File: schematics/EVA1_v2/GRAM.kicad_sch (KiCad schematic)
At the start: 8 parts, among them U11 CY62256-70PC, U25 74LS157, U26 74LS157, U27 74LS157, U28 74LS157, U35 74LS165, U36 74LS245, U38 74LS573

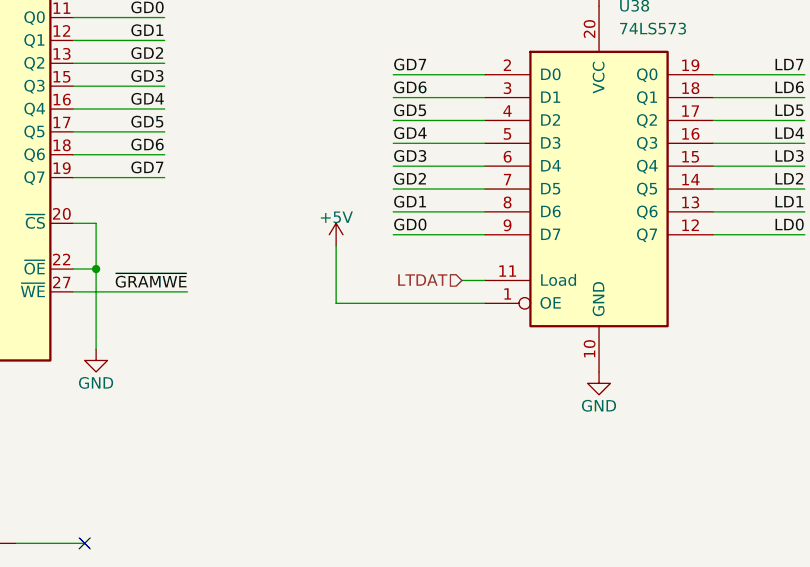
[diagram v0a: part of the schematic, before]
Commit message: schematics updated
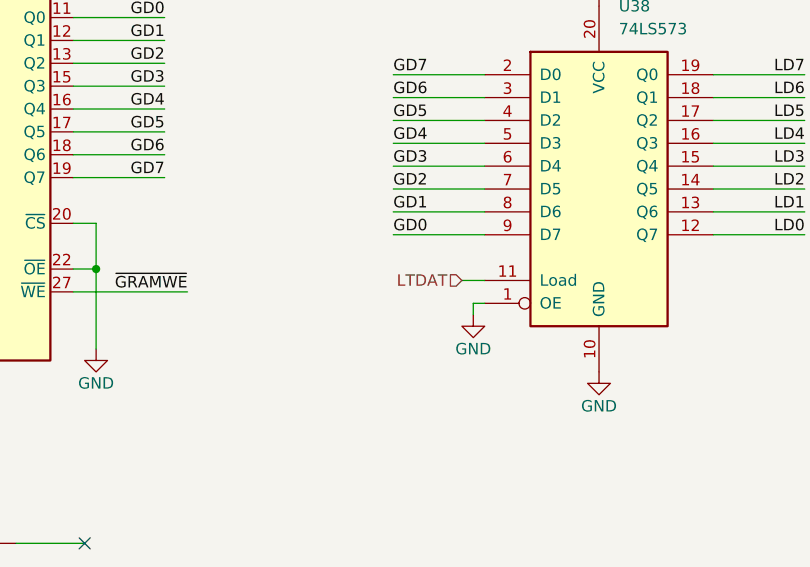
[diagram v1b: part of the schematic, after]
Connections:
- net +5V: no longer U38.1 (OE)
- net GND: now also U38.1 (OE)
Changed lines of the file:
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@@
 		(title "EVA1 (Epson Video Adapter) - Graphic RAM")
 		(date "2025-01-09")
-		(rev "v0.1")
+		(rev "v0.3")
 		(company "100% Offner")
 		(comment 1 "v0.1: Initial Release")
+		(comment 2 "v0.2: Production version")
+		(comment 3 "v0.3: Redesign with SRAM")
 	)
 	(junction
@@
 	(wire
 		(pts
-			(xy 226.06 55.88) (xy 209.55 55.88)
+			(xy 226.06 55.88) (xy 224.79 55.88)
 		)
 		(stroke
@@
 	(wire
 		(pts
-			(xy 209.55 49.53) (xy 209.55 55.88)
-		)
-		(stroke
-			(width 0)
-			(type default)
-		)
-	)
-	(wire
-		(pts
 			(xy 180.34 24.13) (xy 190.5 24.13)
 		)
@@
 	(wire
 		(pts
+			(xy 224.79 55.88) (xy 224.79 57.15)
+		)
+		(stroke
+			(width 0)
+			(type default)
+		)
+	)
+	(wire
+		(pts
 			(xy 180.34 54.61) (xy 193.04 54.61)
 		)
@@
 	(symbol
 		(lib_id "power:GND")
+		(at 224.79 57.15 0)
+		(unit 1)
+		(exclude_from_sim no)
+		(in_bom yes)
+		(on_board yes)
+		(dnp no)
+		(property "Reference" "#PWR70"
+			(at 224.79 63.5 0)
+			(effects
+				(font
+					(size 1.27 1.27)
+				)
+				(hide yes)
+			)
+		)
+		(property "Value" "GND"
+			(at 224.79 60.96 0)
+			(effects
+				(font
+					(size 1.27 1.27)
+				)
+			)
+		)
+		(property "Footprint" ""
+			(at 224.79 57.15 0)
+			(effects
+				(font
+					(size 1.27 1.27)
+				)
+				(hide yes)
+			)
+		)
+		(property "Datasheet" ""
+			(at 224.79 57.15 0)
+			(effects
+				(font
+					(size 1.27 1.27)
+				)
+				(hide yes)
+			)
+		)
+		(property "Description" ""
+			(at 224.79 57.15 0)
+			(effects
+				(font
+					(size 1.27 1.27)
+				)
+				(hide yes)
+			)
+		)
+		(pin "1"
+		)
+		(instances
+			(project "EVA1_v2"
+				(path "/5be3a086-9309-43f4-b37c-0519e88c3e26/4b69d599-71e1-4fe9-8a9f-9911911cdfa3"
+					(reference "#PWR70")
+					(unit 1)
+				)
+			)
+		)
+	)
+	(symbol
+		(lib_id "power:GND")
 		(at 114.3 67.31 0)
 		(unit 1)
@@
 					(unit 1)
 				)
-			)
-		)
-	)
-	(symbol
-		(lib_id "power:+5V")
-		(at 209.55 49.53 0)
-		(unit 1)
-		(exclude_from_sim no)
-		(in_bom yes)
-		(on_board yes)
-		(dnp no)
-		(property "Reference" "#PWR162"
-			(at 209.55 53.34 0)
-			(effects
-				(font
-					(size 1.27 1.27)
-				)
-				(hide yes)
-			)
-		)
-		(property "Value" "+5V"
-			(at 209.55 46.355 0)
-			(effects
-				(font
-					(size 1.27 1.27)
-				)
-			)
-		)
-		(property "Footprint" ""
-			(at 209.55 49.53 0)
-			(effects
-				(font
-					(size 1.27 1.27)
-				)
-				(hide yes)
-			)
-		)
-		(property "Datasheet" ""
-			(at 209.55 49.53 0)
-			(effects
-				(font
-					(size 1.27 1.27)
-				)
-				(hide yes)
-			)
-		)
-		(property "Description" ""
-			(at 209.55 49.53 0)
-			(effects
-				(font
-					(size 1.27 1.27)
-				)
-				(hide yes)
-			)
-		)
-		(pin "1"
-		)
-		(instances
-			(project "EVA1_v2"
-				(path "/5be3a086-9309-43f4-b37c-0519e88c3e26/4b69d599-71e1-4fe9-8a9f-9911911cdfa3"
-					(reference "#PWR162")
-					(unit 1)
-				)

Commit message: Schematic and Board updated
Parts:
- U25, U26, U27, U28: value 74LS157 -> 74ALS157
- U35: value 74LS165 -> 74HCT165
- U36: value 74LS245 -> 74HCT245
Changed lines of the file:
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@@
 			)
 		)
-		(property "Value" "74LS157"
+		(property "Value" "74ALS157"
 			(at 119.0341 128.27 0)
 			(effects
@@
 			)
 		)
-		(property "Value" "74LS245"
+		(property "Value" "74HCT245"
 			(at 211.7441 105.41 0)
 			(effects
@@
 			)
 		)
-		(property "Value" "74LS157"
+		(property "Value" "74ALS157"
 			(at 163.4841 78.74 0)
 			(effects
@@
 			)
 		)
-		(property "Value" "74LS157"
+		(property "Value" "74ALS157"
 			(at 116.4941 22.86 0)
 			(effects
@@
 			)
 		)
-		(property "Value" "74LS157"
+		(property "Value" "74ALS157"
 			(at 112.6841 77.47 0)
 			(effects
@@
 			)
 		)
-		(property "Value" "74LS165"
+		(property "Value" "74HCT165"
 			(at 265.0841 113.03 0)
 			(effects

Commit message: new Gerber files
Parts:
- removed U38: 74LS573, Package_DIP:DIP-20_W7.62mm, symbol 74xx:74LS573
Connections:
- net LD0 is gone; now on net GD0: U35.11 (D0)
- net LD1 is gone; now on net GD1: U35.12 (D1)
- net LD2 is gone; now on net GD2: U35.13 (D2)
- net LD3 is gone; now on net GD3: U35.14 (D3)
- net LD4 is gone; now on net GD4: U35.3 (D4)
- net LD5 is gone; now on net GD5: U35.4 (D5)
- net LD6 is gone; now on net GD6: U35.5 (D6)
- net LD7 is gone; now on net GD7: U35.6 (D7)
